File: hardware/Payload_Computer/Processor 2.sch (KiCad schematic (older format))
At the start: 1 part

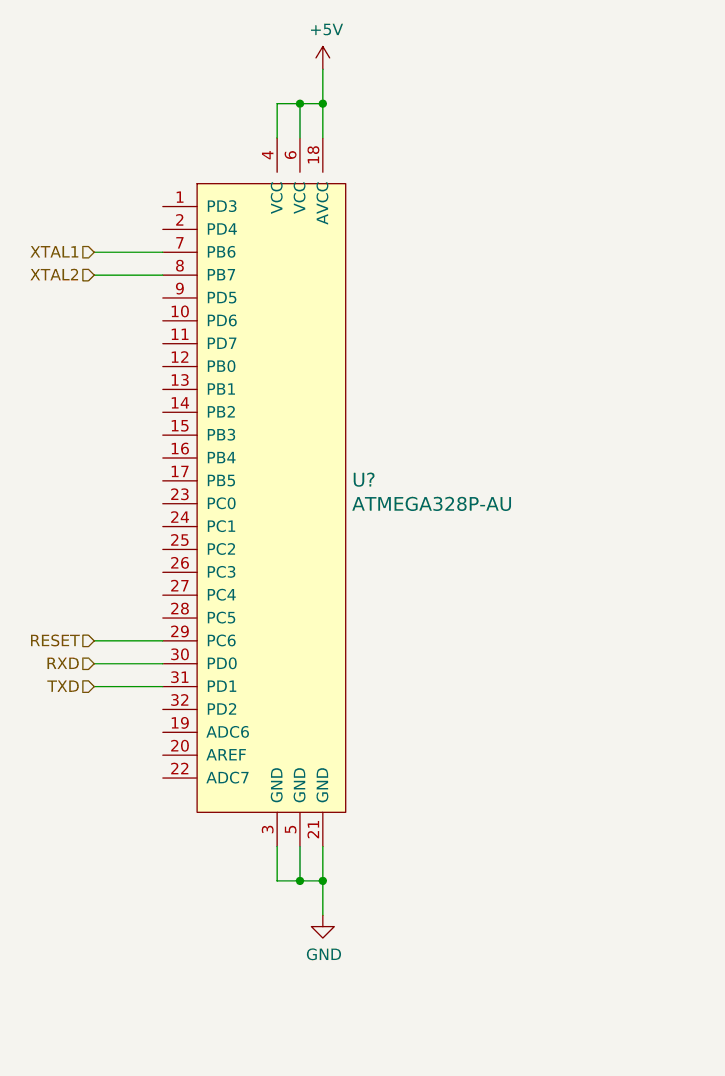
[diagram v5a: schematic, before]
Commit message: Finished ICSP. Added a few leds and filtering caps
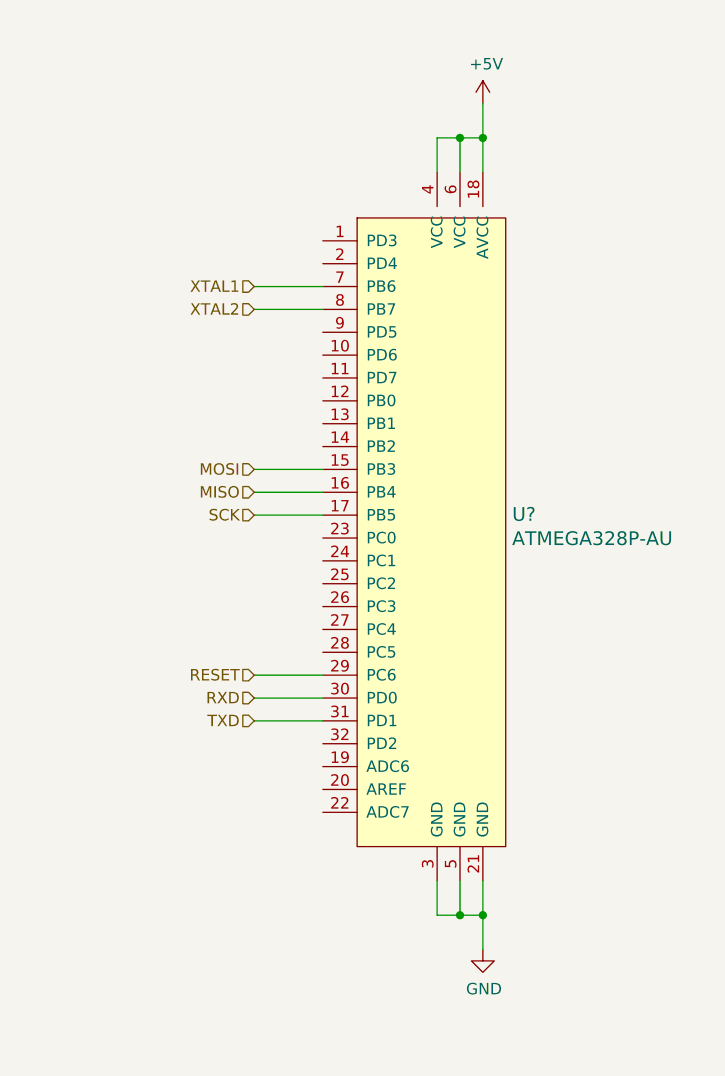
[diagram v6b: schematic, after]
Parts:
- removed U?: ATMEGA328P-AU, digikey-footprints:TQFP-32_7x7mm, symbol dk_Embedded-Microcontrollers:ATMEGA328P-AU
- added U?: ATMEGA328P-AU, digikey-footprints:TQFP-32_7x7mm, symbol dk_Embedded-Microcontrollers:ATMEGA328P-AU
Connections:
- net +5V: now also U?.18 (AVCC), U?.4 (VCC), U?.6 (VCC)
- net GND: now also U?.21 (GND), U?.3 (GND), U?.5 (GND)
- net RESET: now also U?.29 (PC6)
- net RXD: now also U?.30 (PD0)
- net TXD: now also U?.31 (PD1)
- net XTAL1: now also U?.7 (PB6)
- net XTAL2: now also U?.8 (PB7)
- new net MISO: U?.16 (PB4)
- new net MOSI: U?.15 (PB3)
- new net SCK: U?.17 (PB5)
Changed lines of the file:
@@
 $Descr A4 11693 8268
 encoding utf-8
-Sheet 3 11
+Sheet 3 13
 Title ""
 Date ""
@@
 $Comp
 L dk_Embedded-Microcontrollers:ATMEGA328P-AU U?
-U 1 1 5F8DCE4B
-P 5500 3550
-F 0 "U?" H 5828 3653 60  0000 L CNN
-F 1 "ATMEGA328P-AU" H 5828 3547 60  0000 L CNN
-F 2 "digikey-footprints:TQFP-32_7x7mm" H 5700 3750 60  0001 L CNN
-F 3 "http://www.microchip.com/mymicrochip/filehandler.aspx?ddocname=en608326" H 5700 3850 60  0001 L CNN
-F 4 "ATMEGA328P-AU-ND" H 5700 3950 60  0001 L CNN "Digi-Key_PN"
-F 5 "ATMEGA328P-AU" H 5700 4050 60  0001 L CNN "MPN"
-F 6 "Integrated Circuits (ICs)" H 5700 4150 60  0001 L CNN "Category"
-F 7 "Embedded - Microcontrollers" H 5700 4250 60  0001 L CNN "Family"
-F 8 "http://www.microchip.com/mymicrochip/filehandler.aspx?ddocname=en608326" H 5700 4350 60  0001 L CNN "DK_Datasheet_Link"
-F 9 "/product-detail/en/microchip-technology/ATMEGA328P-AU/ATMEGA328P-AU-ND/1832260" H 5700 4450 60  0001 L CNN "DK_Detail_Page"
-F 10 "IC MCU 8BIT 32KB FLASH 32TQFP" H 5700 4550 60  0001 L CNN "Description"
-F 11 "Microchip Technology" H 5700 4650 60  0001 L CNN "Manufacturer"
-F 12 "Active" H 5700 4750 60  0001 L CNN "Status"
-	1    5500 3550
+U 1 1 5F97FCE7
+P 6200 3700
+AR Path="/5F8457E8/5F97FCE7" Ref="U?"  Part="1"
+AR Path="/5F84585C/5F97FCE7" Ref="U?"  Part="1"
+F 0 "U?" H 6528 3803 60  0000 L CNN
+F 1 "ATMEGA328P-AU" H 6528 3697 60  0000 L CNN
+F 2 "digikey-footprints:TQFP-32_7x7mm" H 6400 3900 60  0001 L CNN
+F 3 "http://www.microchip.com/mymicrochip/filehandler.aspx?ddocname=en608326" H 6400 4000 60  0001 L CNN
+F 4 "ATMEGA328P-AU-ND" H 6400 4100 60  0001 L CNN "Digi-Key_PN"
+F 5 "ATMEGA328P-AU" H 6400 4200 60  0001 L CNN "MPN"
+F 6 "Integrated Circuits (ICs)" H 6400 4300 60  0001 L CNN "Category"
+F 7 "Embedded - Microcontrollers" H 6400 4400 60  0001 L CNN "Family"
+F 8 "http://www.microchip.com/mymicrochip/filehandler.aspx?ddocname=en608326" H 6400 4500 60  0001 L CNN "DK_Datasheet_Link"
+F 9 "/product-detail/en/microchip-technology/ATMEGA328P-AU/ATMEGA328P-AU-ND/1832260" H 6400 4600 60  0001 L CNN "DK_Detail_Page"
+F 10 "IC MCU 8BIT 32KB FLASH 32TQFP" H 6400 4700 60  0001 L CNN "Description"
+F 11 "Microchip Technology" H 6400 4800 60  0001 L CNN "Manufacturer"
+F 12 "Active" H 6400 4900 60  0001 L CNN "Status"
+	1    6200 3700
 	1    0    0    -1
 $EndComp
 $Comp
 L power:+5V #PWR?
-U 1 1 5F8DCE51
-P 5700 1650
-F 0 "#PWR?" H 5700 1500 50  0001 C CNN
-F 1 "+5V" H 5715 1823 50  0000 C CNN
-F 2 "" H 5700 1650 50  0001 C CNN
-F 3 "" H 5700 1650 50  0001 C CNN
-	1    5700 1650
+U 1 1 5F97FCED
+P 6400 1800
+AR Path="/5F8457E8/5F97FCED" Ref="#PWR?"  Part="1"
+AR Path="/5F84585C/5F97FCED" Ref="#PWR0103"  Part="1"
+F 0 "#PWR0103" H 6400 1650 50  0001 C CNN
+F 1 "+5V" H 6415 1973 50  0000 C CNN
+F 2 "" H 6400 1800 50  0001 C CNN
+F 3 "" H 6400 1800 50  0001 C CNN
+	1    6400 1800
 	1    0    0    -1
 $EndComp
 Wire Wire Line
-	5700 1950 5700 1800
+	6400 2100 6400 1950
 Wire Wire Line
-	5600 1950 5600 1800
+	6300 2100 6300 1950
 Wire Wire Line
-	5600 1800 5700 1800
-Connection ~ 5700 1800
+	6300 1950 6400 1950
+Connection ~ 6400 1950
 Wire Wire Line
-	5700 1800 5700 1650
+	6400 1950 6400 1800
 Wire Wire Line
-	5500 1950 5500 1800
+	6200 2100 6200 1950
 Wire Wire Line
-	5500 1800 5600 1800
-Connection ~ 5600 1800
+	6200 1950 6300 1950
+Connection ~ 6300 1950
 $Comp
 L power:GND #PWR?
-U 1 1 5F8DCE5F
-P 5700 5350
-F 0 "#PWR?" H 5700 5100 50  0001 C CNN
-F 1 "GND" H 5705 5177 50  0000 C CNN
-F 2 "" H 5700 5350 50  0001 C CNN
-F 3 "" H 5700 5350 50  0001 C CNN
-	1    5700 5350
+U 1 1 5F97FCFB
+P 6400 5500
+AR Path="/5F8457E8/5F97FCFB" Ref="#PWR?"  Part="1"
+AR Path="/5F84585C/5F97FCFB" Ref="#PWR0104"  Part="1"
+F 0 "#PWR0104" H 6400 5250 50  0001 C CNN
+F 1 "GND" H 6405 5327 50  0000 C CNN
+F 2 "" H 6400 5500 50  0001 C CNN
+F 3 "" H 6400 5500 50  0001 C CNN
+	1    6400 5500
 	1    0    0    -1
 $EndComp
 Wire Wire Line
-	5700 5050 5700 5200
+	6400 5200 6400 5350
 Wire Wire Line
-	5600 5050 5600 5200
+	6300 5200 6300 5350
 Wire Wire Line
-	5600 5200 5700 5200
-Connection ~ 5700 5200
+	6300 5350 6400 5350
+Connection ~ 6400 5350
 Wire Wire Line
-	5700 5200 5700 5350
+	6400 5350 6400 5500
 Wire Wire Line
-	5500 5050 5500 5200
+	6200 5200 6200 5350
 Wire Wire Line
-	5500 5200 5600 5200
-Connection ~ 5600 5200
-Text HLabel 4700 2450 0    50   Input ~ 0
+	6200 5350 6300 5350
+Connection ~ 6300 5350
+Text HLabel 5400 2600 0    50   Input ~ 0
 XTAL1
-Text HLabel 4700 2550 0    50   Input ~ 0
+Text HLabel 5400 2700 0    50   Input ~ 0
 XTAL2
 Wire Wire Line
-	4700 2450 5000 2450
+	5400 2600 5700 2600
 Wire Wire Line
-	4700 2550 5000 2550
-Text HLabel 4700 4350 0    50   Input ~ 0
+	5400 2700 5700 2700
+Text HLabel 5400 4500 0    50   Input ~ 0
 TXD
-Text HLabel 4700 4250 0    50   Input ~ 0
+Text HLabel 5400 4400 0    50   Input ~ 0
 RXD
 Wire Wire Line
-	4700 4250 5000 4250
+	5400 4400 5700 4400
 Wire Wire Line
-	4700 4350 5000 4350
-Text HLabel 4700 4150 0    50   Input ~ 0
+	5400 4500 5700 4500
+Text HLabel 5400 4300 0    50   Input ~ 0
 RESET
 Wire Wire Line
-	4700 4150 5000 4150
+	5400 4300 5700 4300
+Text HLabel 5400 3400 0    50   Input ~ 0
+MOSI
+Text HLabel 5400 3500 0    50   Input ~ 0
+MISO
+Text HLabel 5400 3600 0    50   Input ~ 0
+SCK
+Wire Wire Line
+	5400 3400 5700 3400
+Wire Wire Line
+	5700 3500 5400 3500
+Wire Wire Line
+	5400 3600 5700 3600
 $EndSCHEMATC
